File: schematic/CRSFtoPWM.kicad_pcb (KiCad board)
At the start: 4 copper layers, 40 x 21 mm, 30 parts, among them J1 Bat+, J2 UART1/Rx, J3 ICSP, J4 TSW-104-08-G-T-RA, J5 TSW-104-08-G-T-RA, J6 TSW-104-08-G-T-RA, J7 TSW-102-08-L-T-RA, U1 AP7375-50W5-7, U2 AP2210N-3.3TRG1, U3 ATSAMD21E18A-MU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

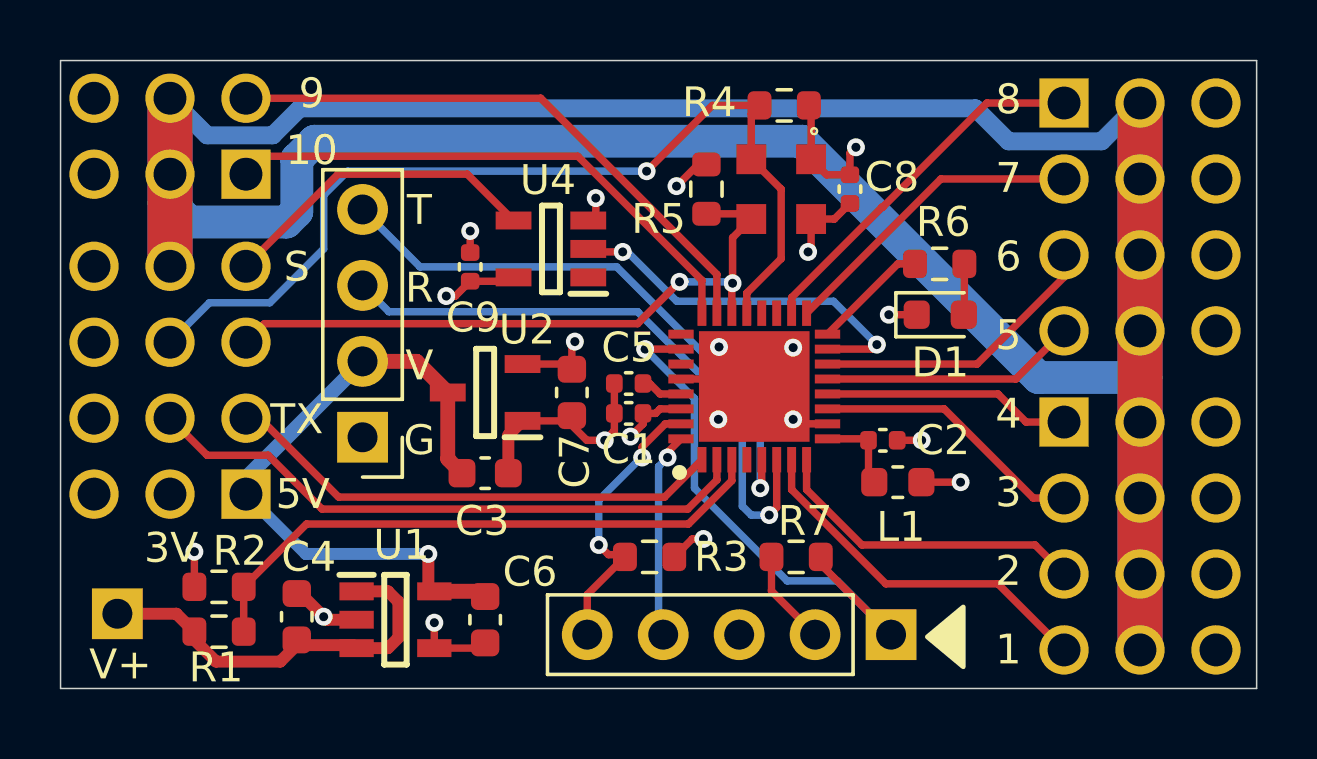
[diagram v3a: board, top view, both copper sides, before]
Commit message: Added jumper to allow power from VServo
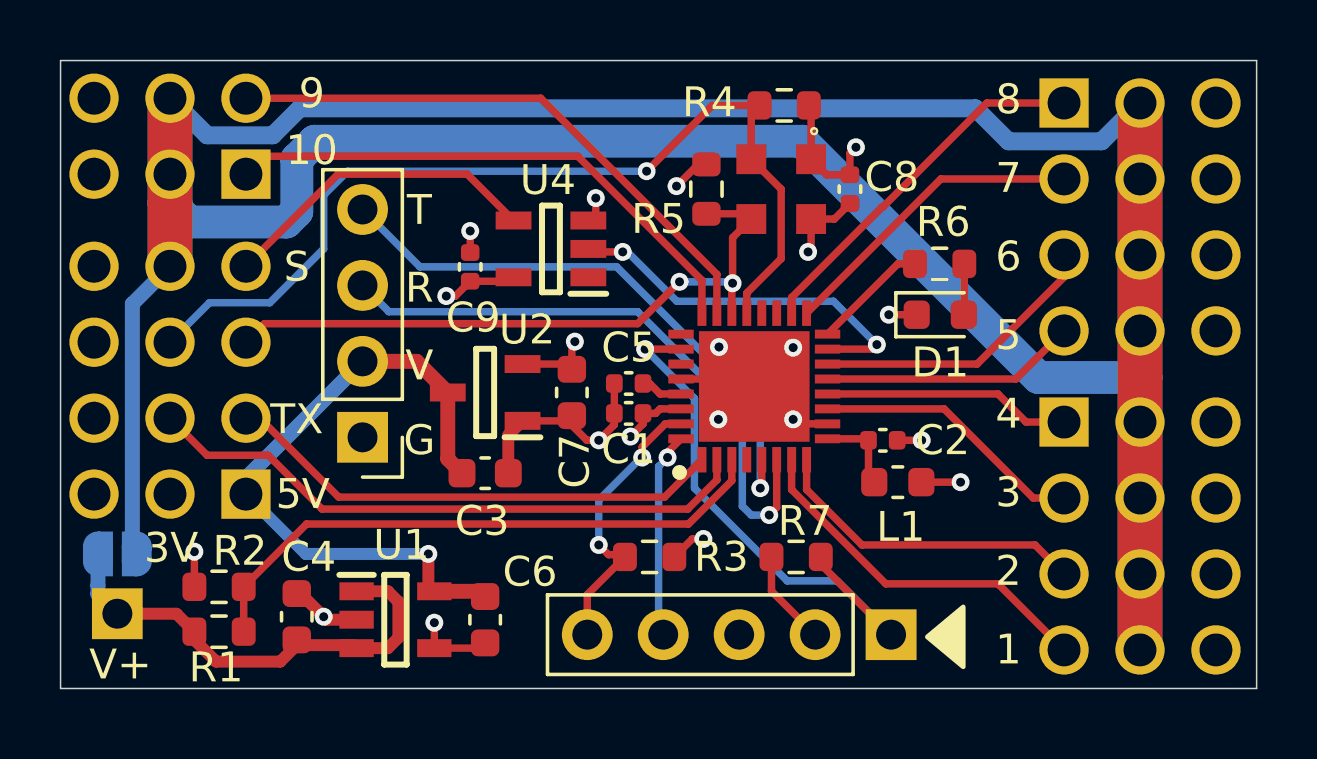
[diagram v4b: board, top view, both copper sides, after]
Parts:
- added JP1: SolderJumper_2_Open, Jumper:SolderJumper-2_P1.3mm_Open_RoundedPad1.0x1.5mm, B.Cu at (142.9, 111.1)
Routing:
- net Vservo: track 120.3 -> 130.5 mm
- net Vbat: track 13.0 -> 15.2 mm
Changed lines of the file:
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@@
     )
+  )
+  (footprint "Jumper:SolderJumper-2_P1.3mm_Open_RoundedPad1.0x1.5mm" (layer "B.Cu")
+    (at 142.9 111.1)
+    (descr "SMD Solder Jumper, 1x1.5mm, rounded Pads, 0.3mm gap, open")
+    (tags "solder jumper open")
+    (property "Sheetfile" "CRSFtoPWM.kicad_sch")
+    (property "Sheetname" "")
+    (attr exclude_from_pos_files)
+    (fp_text reference "JP1" (at 2.8 -0.1) (layer "B.SilkS")
+      (effects (font (size 1 1) (thickness 0.15)) (justify mirror))
+    )
+    (fp_text value "SolderJumper_2_Open" (at 0 -1.9) (layer "B.Fab")
+      (effects (font (size 1 1) (thickness 0.15)) (justify mirror))
+    )
+    (fp_line (start -0.7 1) (end 0.7 1) (layer "B.SilkS") (width 0.12))
+    (fp_line (start 1.4 0.3) (end 1.4 -0.3) (layer "B.SilkS") (width 0.12))
+    (fp_line (start -1.4 -0.3) (end -1.4 0.3) (layer "B.SilkS") (width 0.12))
+    (fp_line (start 0.7 -1) (end -0.7 -1) (layer "B.SilkS") (width 0.12))
+    (fp_arc (start 1.4 0.3) (mid 1.194975 0.794975) (end 0.7 1) (layer "B.SilkS") (width 0.12))
+    (fp_arc (start -1.4 -0.3) (mid -1.194975 -0.794975) (end -0.7 -1) (layer "B.SilkS") (width 0.12))
+    (fp_arc (start 0.7 -1) (mid 1.194975 -0.794975) (end 1.4 -0.3) (layer "B.SilkS") (width 0.12))
+    (fp_arc (start -0.7 1) (mid -1.194975 0.794975) (end -1.4 0.3) (layer "B.SilkS") (width 0.12))
+    (fp_line (start -1.65 1.25) (end -1.65 -1.25) (layer "B.CrtYd") (width 0.05))
+    (fp_line (start 1.65 -1.25) (end -1.65 -1.25) (layer "B.CrtYd") (width 0.05))
+    (fp_line (start 1.65 -1.25) (end 1.65 1.25) (layer "B.CrtYd") (width 0.05))
+    (fp_line (start -1.65 1.25) (end 1.65 1.25) (layer "B.CrtYd") (width 0.05))
+    (pad "1" smd custom (at -0.65 0) (size 1 0.5) (layers "B.Cu" "B.Mask")
+      (net 3 "Vbat") (pinfunction "A") (pintype "passive") (zone_connect 2)
+      (options (clearance outline) (anchor rect))
+      (primitives
+        (gr_circle (center 0 -0.25) (end 0.5 -0.25) (width 0) (fill yes))
+        (gr_circle (center 0 0.25) (end 0.5 0.25) (width 0) (fill yes))
+        (gr_poly (pts
+            (xy 0.5 -0.75)
+            (xy 0 -0.75)
+            (xy 0 0.75)
+            (xy 0.5 0.75)
+          ) (width 0) (fill yes))
+      ))
+    (pad "2" smd custom (at 0.65 0) (size 1 0.5) (layers "B.Cu" "B.Mask")
+      (net 29 "Vservo") (pinfunction "B") (pintype "passive") (zone_connect 2)
+      (options (clearance outline) (anchor rect))
+      (primitives
+        (gr_circle (center 0 -0.25) (end 0.5 -0.25) (width 0) (fill yes))
+        (gr_circle (center 0 0.25) (end 0.5 0.25) (width 0) (fill yes))
+        (gr_poly (pts
+            (xy 0 -0.75)
+            (xy -0.5 -0.75)
+            (xy -0.5 0.75)
+            (xy 0 0.75)
+          ) (width 0) (fill yes))
+      ))
   )
   (gr_poly
@@
   (segment (start 144.875 113.1) (end 145.475 113.7) (width 0.4) (layer "F.Cu") (net 3))
   (segment (start 142.9 113.1) (end 144.875 113.1) (width 0.4) (layer "F.Cu") (net 3))
+  (segment (start 142.25 111.1) (end 142.25 112.15) (width 0.5) (layer "B.Cu") (net 3))
+  (segment (start 142.25 112.15) (end 142.25 112.45) (width 0.5) (layer "B.Cu") (net 3))
+  (segment (start 142.25 112.45) (end 142.9 113.1) (width 0.5) (layer "B.Cu") (net 3))
   (segment (start 160.48 105.4) (end 160.7 105.4) (width 0.25) (layer "F.Cu") (net 4))
   (segment (start 161.05 105.75) (end 161.75 105.75) (width 0.25) (layer "F.Cu") (net 4))
@@
   (segment (start 177.1 96.02) (end 177.1 105.2) (width 1.5) (layer "B.Cu") (net 29))
   (segment (start 148.55 100) (end 148.9 99.65) (width 1.1) (layer "B.Cu") (net 29))
+  (segment (start 143.55 111.1) (end 143.4 110.95) (width 0.4) (layer "B.Cu") (net 29))
   (segment (start 145.3 100) (end 148.55 100) (width 1.1) (layer "B.Cu") (net 29))
   (segment (start 148.9 97.9) (end 149.50025 97.29975) (width 1.1) (layer "B.Cu") (net 29))
@@
   (segment (start 149 96.2) (end 148.1 97.1) (width 0.6) (layer "B.Cu") (net 29))
   (segment (start 144.66 95.86) (end 144.66 99.36) (width 1.5) (layer "B.Cu") (net 29))
+  (segment (start 143.4 110.95) (end 143.4 102.74) (width 0.5) (layer "B.Cu") (net 29))
   (segment (start 173.7 105.2) (end 177.1 105.2) (width 1.1) (layer "B.Cu") (net 29))
   (segment (start 149.50025 97.29975) (end 165.79975 97.29975) (width 1.1) (layer "B.Cu") (net 29))
@@
   (segment (start 177.1 96.02) (end 175.82 97.3) (width 0.6) (layer "B.Cu") (net 29))
   (segment (start 144.66 99.36) (end 145.3 100) (width 1.1) (layer "B.Cu") (net 29))
+  (segment (start 143.4 102.74) (end 144.66 101.48) (width 0.5) (layer "B.Cu") (net 29))
   (segment (start 148.1 97.1) (end 145.9 97.1) (width 0.6) (layer "B.Cu") (net 29))
-  (segment (start 158.1 106.8) (end 158.6 107.3) (width 0.25) (layer "F.Cu") (net 30))
   (segment (start 168.98 107.3) (end 169.8 107.3) (width 0.25) (layer "F.Cu") (net 30))
   (segment (start 145.475 112.2) (end 145.475 111.025) (width 0.25) (layer "F.Cu") (net 30))
   (segment (start 158.9 99.732916) (end 158.9 99.2) (width 0.25) (layer "F.Cu") (net 30))
   (segment (start 159.52 106.4) (end 159.52 105.4) (width 0.25) (layer "F.Cu") (net 30))
-  (segment (start 159.52 106.98) (end 159.2 107.3) (width 0.25) (layer "F.Cu") (net 30))
+  (segment (start 158.6 107.3) (end 159 107.3) (width 0.25) (layer "F.Cu") (net 30))
   (segment (start 165.938464 106.75) (end 165.7245 106.536036) (width 0.25) (layer "F.Cu") (net 30))
   (segment (start 153.5 114.25) (end 153.5 113.4) (width 0.25) (layer "F.Cu") (net 30))
+  (segment (start 159.52 106.78) (end 159 107.3) (width 0.25) (layer "F.Cu") (net 30))
   (segment (start 153.5 114.25) (end 155.025 114.25) (width 0.25) (layer "F.Cu") (net 30))
   (segment (start 168.7 103.1) (end 169.6325 103.1) (width 0.25) (layer "F.Cu") (net 30))
-  (segment (start 159.52 106.4) (end 159.52 106.98) (width 0.25) (layer "F.Cu") (net 30))
   (segment (start 149.9 113.3) (end 150.9 113.3) (width 0.4) (layer "F.Cu") (net 30))
   (segment (start 166.65 106.75) (end 165.938464 106.75) (width 0.25) (layer "F.Cu") (net 30))
@@
   (segment (start 158.682916 99.95) (end 158.9 99.732916) (width 0.25) (layer "F.Cu") (net 30))
   (segment (start 166.1 99.9) (end 166.1 100.9) (width 0.25) (layer "F.Cu") (net 30))
-  (segment (start 158.6 107.3) (end 159.2 107.3) (width 0.25) (layer "F.Cu") (net 30))
+  (segment (start 159.52 106.4) (end 159.52 106.78) (width 0.25) (layer "F.Cu") (net 30))
+  (segment (start 158.1 106.8) (end 158.6 107.3) (width 0.25) (layer "F.Cu") (net 30))
   (segment (start 166.88 99.9) (end 167.4 99.38) (width 0.25) (layer "F.Cu") (net 30))
   (segment (start 154.7 101.02) (end 154.7 100.3) (width 0.25) (layer "F.Cu") (net 30))
@@
   (via (at 158.9 99.2) (size 0.6) (drill 0.3) (layers "F.Cu" "B.Cu") (net 30))
   (via (at 163.020878 104.179122) (size 0.6) (drill 0.3) (layers "F.Cu" "B.Cu") (net 30))
-  (via (at 159.2 107.3) (size 0.6) (drill 0.3) (layers "F.Cu" "B.Cu") (net 30))
+  (via (at 159 107.3) (size 0.6) (drill 0.3) (layers "F.Cu" "B.Cu") (net 30))
   (via (at 149.8 113.2) (size 0.6) (drill 0.3) (layers "F.Cu" "B.Cu") (net 30))
   (via (at 145.475 111.025) (size 0.6) (drill 0.3) (layers "F.Cu" "B.Cu") (net 30))
